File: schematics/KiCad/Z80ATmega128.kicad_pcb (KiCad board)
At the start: 2 copper layers, 139.7 x 100.3 mm, 90 parts, among them J1 AVR-ISP-6, J2 Serial I/O, J3 DC 5V, J4 DC 5V, J5 Z80[1..20], J6 Micro_SD_Card_Det_Hirose_DM3AT, J7 Z80[21..40], SW1 RESET, SW2 POWER, U1 74HC08, U10 74HC32, U11 74HC4050, U12 LP2950-3.3, U13 74HC74, U2 74HC04, U3 74HC125, U4 74AC573, U5 74HC574, U6 74HC125, U7 74HC244, U8 74HC245, U9 74HC32, Y1 16MHz, Y2 8MHz

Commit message: Update schematics for Z80 /HALT and /NMI.
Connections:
- CPU2 pad 16: unconnected-(CPU2-Pad16) -> /NMI
- CPU2 pad 17: unconnected-(CPU2-Pad17) -> /HALT

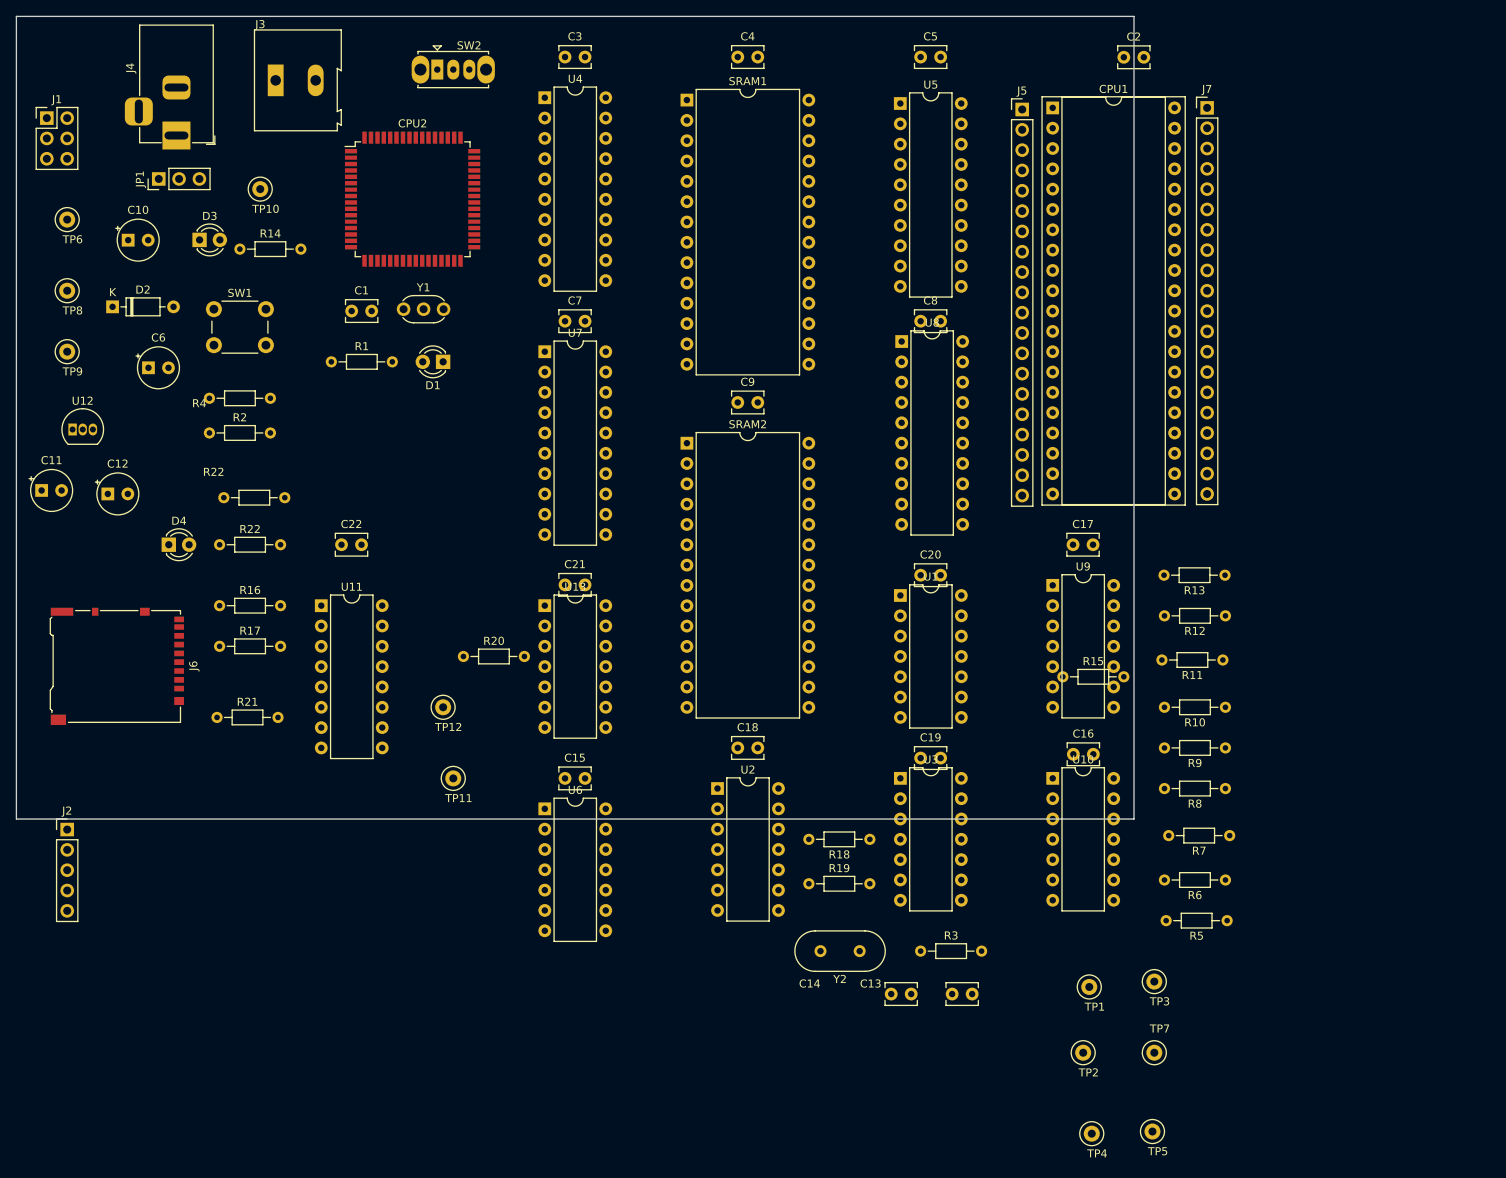
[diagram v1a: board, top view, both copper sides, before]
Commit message: Update schematics.
Separate reset and SD card interface as different layer.
Power on/manual reset are isolated from ISP /RST for stability.
XMEM /RD(PG1) and /WR(PG0) were swapped.
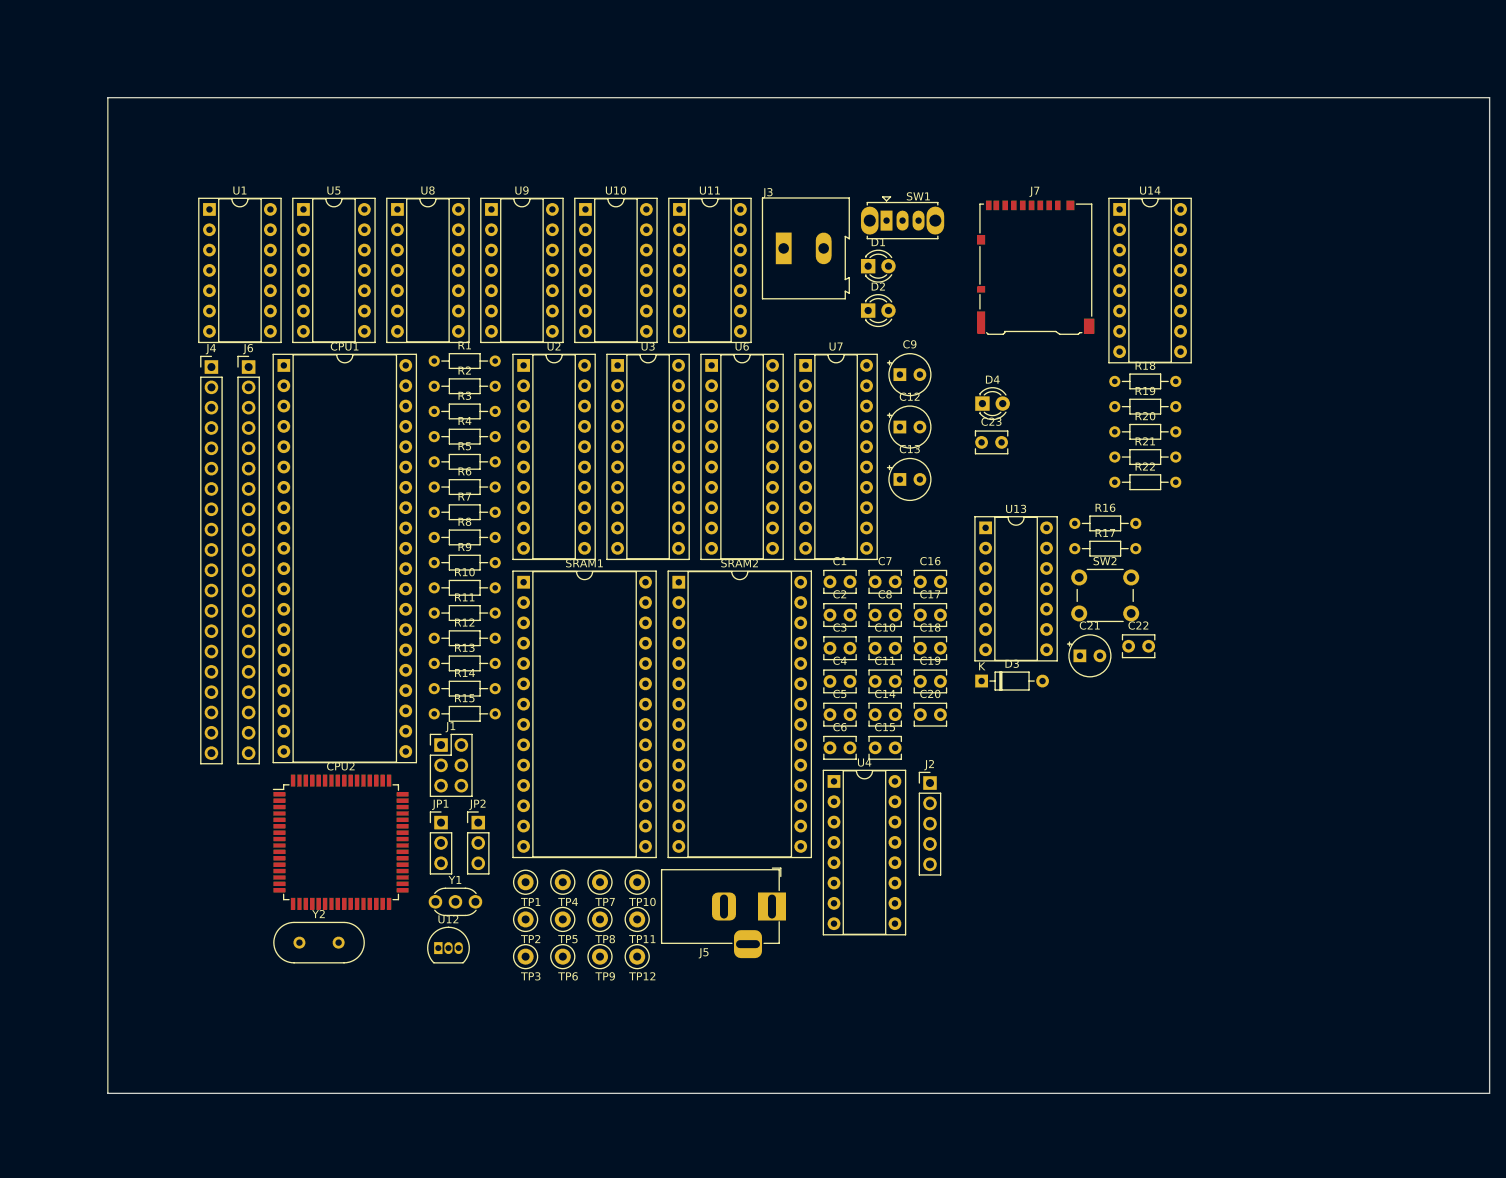
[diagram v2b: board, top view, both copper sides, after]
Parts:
- removed the R22 at (40.6, 81.3)
- removed the R22 at (41.2, 75.4)
- added C23: 0.1u, Capacitor_THT:C_Disc_D3.8mm_W2.6mm_P2.50mm, F.Cu at (135.9, 68.5)
- added JP2: DC-IN SEL, Connector_PinHeader_2.54mm:PinHeader_1x03_P2.54mm_Vertical, F.Cu at (73.0, 116.0)
- added R22: 1K, Resistor_THT:R_Axial_DIN0204_L3.6mm_D1.6mm_P7.62mm_Horizontal, F.Cu at (152.5, 73.5)
- added U14: 74HC4050, Package_DIP:DIP-16_W7.62mm_Socket, F.Cu at (153.1, 39.4)
- C10: value 100u -> 22p; footprint Capacitor_THT:CP_Radial_Tantal_D5.0mm_P2.50mm -> Capacitor_THT:C_Disc_D3.8mm_W2.6mm_P2.50mm
- C11: value 1u -> 22p; footprint Capacitor_THT:CP_Radial_Tantal_D5.0mm_P2.50mm -> Capacitor_THT:C_Disc_D3.8mm_W2.6mm_P2.50mm
- C13: value 22p -> 1u; footprint Capacitor_THT:C_Disc_D3.8mm_W2.6mm_P2.50mm -> Capacitor_THT:CP_Radial_Tantal_D5.0mm_P2.50mm
- C14: value 22p -> 0.1u
- C21: value 0.1u -> 47u; footprint Capacitor_THT:C_Disc_D3.8mm_W2.6mm_P2.50mm -> Capacitor_THT:CP_Radial_Tantal_D5.0mm_P2.50mm
- C6: value 1u -> 0.1u; footprint Capacitor_THT:CP_Radial_Tantal_D5.0mm_P2.50mm -> Capacitor_THT:C_Disc_D3.8mm_W2.6mm_P2.50mm
- C9: value 0.1u -> 100u; footprint Capacitor_THT:C_Disc_D3.8mm_W2.6mm_P2.50mm -> Capacitor_THT:CP_Radial_Tantal_D5.0mm_P2.50mm
- D1: value DMA -> POWER
- D2: value 1N4148 -> Z80 active; footprint Diode_THT:D_DO-35_SOD27_P7.62mm_Horizontal -> LED_THT:LED_D3.0mm
- D3: value POWER -> 1N4148; footprint LED_THT:LED_D3.0mm -> Diode_THT:D_DO-35_SOD27_P7.62mm_Horizontal
- J4: value DC 5V -> Z80[1..20]; footprint Connector_BarrelJack:BarrelJack_Horizontal -> Connector_PinHeader_2.54mm:PinHeader_1x20_P2.54mm_Vertical
- J5: value Z80[1..20] -> DC 5V; footprint Connector_PinHeader_2.54mm:PinHeader_1x20_P2.54mm_Vertical -> Connector_BarrelJack:BarrelJack_Horizontal
- J6: value Micro_SD_Card_Det_Hirose_DM3AT -> Z80[21..40]; footprint Connector_Card:microSD_HC_Hirose_DM3AT-SF-PEJM5 -> Connector_PinHeader_2.54mm:PinHeader_1x20_P2.54mm_Vertical
- J7: value Z80[21..40] -> Micro_SD_Card_Det_Hirose_DM3AT; footprint Connector_PinHeader_2.54mm:PinHeader_1x20_P2.54mm_Vertical -> Connector_Card:microSD_HC_Hirose_DM3AT-SF-PEJM5
- JP1: value DC-IN SEL -> Disable Z80
- R1: value 1K -> 10K
- R11, R15: value 10K -> 1K
- R13: value 10K -> 1M
- R14: value 1K -> 100
- R17: value 10K -> 100
- R18: value 1M -> 10K
- R19, R4: value 100 -> 10K
- SRAM1, SRAM2: footprint Package_DIP:DIP-28_W15.24mm -> Package_DIP:DIP-28_W15.24mm_Socket
- SW1: value RESET -> POWER; footprint Button_Switch_THT:SW_PUSH_6mm_H7.3mm -> Button_Switch_THT:SW_Slide_1P2T_CK_OS102011MS2Q
- SW2: value POWER -> RESET; footprint Button_Switch_THT:SW_Slide_1P2T_CK_OS102011MS2Q -> Button_Switch_THT:SW_PUSH_6mm_H7.3mm
- TP10: value /INTRQ -> /CLRWAIT
- TP12: value /CLRWAIT -> 3.3V
- TP6: value 5V -> /IORD
- TP7: value /IORD -> 5V
- TP8: value GND -> /INTRQ
- TP9: value 3.3V -> GND
- U1: value 74HC08 -> 74HC125; footprint Package_DIP:DIP-14_W7.62mm -> Package_DIP:DIP-14_W7.62mm_Socket
- U10: footprint Package_DIP:DIP-14_W7.62mm -> Package_DIP:DIP-14_W7.62mm_Socket
- U11: value 74HC4050 -> 74HC74; footprint Package_DIP:DIP-16_W7.62mm -> Package_DIP:DIP-14_W7.62mm_Socket
- U13: value 74HC74 -> 74HC132; footprint Package_DIP:DIP-14_W7.62mm -> Package_DIP:DIP-14_W7.62mm_Socket
- U2: value 74HC04 -> 74AC573; footprint Package_DIP:DIP-14_W7.62mm -> Package_DIP:DIP-20_W7.62mm_Socket
- U3: value 74HC125 -> 74HC574; footprint Package_DIP:DIP-14_W7.62mm -> Package_DIP:DIP-20_W7.62mm_Socket
- U4: value 74AC573 -> 74HC04; footprint Package_DIP:DIP-20_W7.62mm -> Package_DIP:DIP-16_W7.62mm_Socket
- U5: value 74HC574 -> 74HC125; footprint Package_DIP:DIP-20_W7.62mm -> Package_DIP:DIP-14_W7.62mm_Socket
- U6: value 74HC125 -> 74HC244; footprint Package_DIP:DIP-14_W7.62mm -> Package_DIP:DIP-20_W7.62mm_Socket
- U7: value 74HC244 -> 74HC245; footprint Package_DIP:DIP-20_W7.62mm -> Package_DIP:DIP-20_W7.62mm_Socket
- U8: value 74HC245 -> 74HC32; footprint Package_DIP:DIP-20_W7.62mm -> Package_DIP:DIP-14_W7.62mm_Socket
- U9: value 74HC32 -> 74HC08; footprint Package_DIP:DIP-14_W7.62mm -> Package_DIP:DIP-14_W7.62mm_Socket
- moved R21 116.8 mm to (152.5, 70.3)
- moved R5 114.5 mm to (67.5, 70.9), turned to 0 degrees
- moved D3 112.2 mm to (135.9, 98.3)
- moved TP6 111.0 mm to (83.5, 132.8)
- moved R6 110.4 mm to (67.5, 74.1), turned to 0 degrees
- moved J2 108.0 mm to (129.4, 111.1)
- moved R17 107.6 mm to (147.5, 81.8)
- moved R16 107.4 mm to (147.5, 78.6)
- moved R7 107.3 mm to (67.5, 77.2), turned to 0 degrees
- moved C11 106.9 mm to (122.6, 98.4)
- moved C10 106.4 mm to (122.6, 94.2)
- moved J5 104.4 mm to (109.7, 126.5)
- moved R8 103.8 mm to (67.5, 80.4), turned to 0 degrees
- moved D4 103.2 mm to (136.0, 63.6)
- moved TP8 103.0 mm to (88.2, 128.1)
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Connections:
- C10 pad 1: VCC -> Net-(C10-Pad1)
- C11 pad 1: VCC -> Net-(C11-Pad1)
- C12 pad 1: +3.3V -> VCC
- C13 pad 1: Net-(C13-Pad1) -> +3.3V
- C14 pad 1: Net-(C14-Pad1) -> VCC
- C21 pad 1: VCC -> Net-(D3-A)
- C22 pad 1: +3.3V -> VCC
- C6 pad 1: Net-(C6-Pad1) -> GND
- C6 pad 2: GND -> VCC
- C9 pad 1: GND -> VCC
- C9 pad 2: VCC -> GND
- CPU1 pad 23: Net-(CPU1-Pad23) -> Net-(CPU1-~{BUSACK})
- CPU1 pad 25: /BUSRQ -> Net-(CPU1-~{BUSRQ})
- CPU1 pad 26: /RESET -> /Z80_RESET
- CPU2 pad 15: /XRESET -> /Reset//Z80_SWRST
- CPU2 pad 2: Net-(CPU2-Pad2) -> Net-(CPU2-PE0)
- CPU2 pad 20: Net-(C6-Pad1) -> /Reset//AVR_RST
- CPU2 pad 3: Net-(CPU2-Pad3) -> Net-(CPU2-PE1)
- CPU2 pad 35: Net-(CPU2-Pad35) -> Net-(CPU2-PC0)
- CPU2 pad 36: Net-(CPU2-Pad36) -> Net-(CPU2-PC1)
- CPU2 pad 37: Net-(CPU2-Pad37) -> Net-(CPU2-PC2)
- CPU2 pad 38: Net-(CPU2-Pad38) -> Net-(CPU2-PC3)
- CPU2 pad 39: Net-(CPU2-Pad39) -> Net-(CPU2-PC4)
- CPU2 pad 40: Net-(CPU2-Pad40) -> Net-(CPU2-PC5)
- CPU2 pad 41: Net-(CPU2-Pad41) -> Net-(CPU2-PC6)
- CPU2 pad 42: Net-(CPU2-Pad42) -> Net-(CPU2-PC7)
- D1 pad 1: Net-(D1-Pad1) -> GND
- D1 pad 2: Net-(D1-Pad2) -> Net-(D1-A)
- D2 pad 1: VCC -> Net-(D2-K)
- D2 pad 2: Net-(C6-Pad1) -> Net-(D2-A)
- D3 pad 1: GND -> VCC
- D3 pad 2: Net-(D3-Pad2) -> Net-(D3-A)
- D4 pad 1: Net-(D4-Pad1) -> Net-(D4-K)
- J1 pad 1: Net-(CPU2-Pad3) -> Net-(CPU2-PE1)
- J1 pad 3: Net-(J1-Pad3) -> Net-(J1-SCK)
- J1 pad 4: Net-(CPU2-Pad2) -> Net-(CPU2-PE0)
- J1 pad 5: Net-(C6-Pad1) -> /Reset//ISP_RST
- J2 pad 1: Net-(J2-Pad1) -> Net-(J2-Pin_1)
- J2 pad 2: Net-(J2-Pad2) -> Net-(J2-Pin_2)
- J3 pad 2: Net-(J3-Pad2) -> Net-(J3-Pin_2)
- J4 pad 1: Net-(J4-Pad1) -> A11
- J4 pad 2: GND -> A12
- J4 pad 3: (no net) -> A13
- J5 pad 1: A11 -> Net-(J5-In)
- J5 pad 2: A12 -> GND
- J5 pad 3: A13 -> (no net)
- J6 pad 1: unconnected-(J6-Pad1) -> A10
- J6 pad 10: GND -> A1
- J6 pad 11: unconnected-(J6-Pad11) -> A0
- J6 pad 2: Net-(D4-Pad1) -> A9
- J6 pad 3: Net-(J6-Pad3) -> A8
- J6 pad 4: +3.3V -> A7
- J6 pad 5: Net-(J6-Pad5) -> A6
- J6 pad 6: GND -> A5
- J6 pad 7: MISO -> A4
- J6 pad 8: unconnected-(J6-Pad8) -> A3
- J6 pad 9: SW -> A2
- J7 pad 1: A10 -> unconnected-(J7-DAT2-Pad1)
- J7 pad 10: A1 -> GND
- J7 pad 11: A0 -> unconnected-(J7-SHIELD-Pad11)
- J7 pad 2: A9 -> Net-(D4-K)
- J7 pad 3: A8 -> Net-(J7-CMD)
- J7 pad 4: A7 -> +3.3V
- J7 pad 5: A6 -> Net-(J7-CLK)
- J7 pad 6: A5 -> GND
- J7 pad 7: A4 -> MISO
- J7 pad 8: A3 -> unconnected-(J7-DAT1-Pad8)
- J7 pad 9: A2 -> SW
- JP1 pad 1: Net-(J4-Pad1) -> GND
- JP1 pad 2: Net-(JP1-Pad2) -> Net-(CPU1-~{BUSRQ})
- JP1 pad 3: Net-(J3-Pad2) -> /BUSRQ
- R1 pad 2: Net-(D1-Pad2) -> /Reset//ISP_RST
- R10 pad 2: /RD -> Net-(CPU1-~{BUSACK})
- R11 pad 1: VCC -> Net-(D1-A)
- R11 pad 2: /WR -> VCC
- R12 pad 2: /BUSRQ -> /CLRWAIT
- R13 pad 1: VCC -> Net-(C11-Pad1)
- R13 pad 2: Net-(CPU1-Pad23) -> Net-(C10-Pad1)
- R14 pad 1: Net-(D3-Pad2) -> Net-(C11-Pad1)
- R14 pad 2: VCC -> Net-(R14-Pad2)
- R15 pad 2: SW -> Net-(D2-A)
- R16 pad 2: /SS -> Net-(D3-A)
- R17 pad 1: MOSI -> Net-(R17-Pad1)
- R17 pad 2: GND -> Net-(D3-A)
- R18 pad 1: Net-(C14-Pad1) -> VCC
- R18 pad 2: Net-(C13-Pad1) -> SW
- R19 pad 1: Net-(C14-Pad1) -> VCC
- R19 pad 2: Net-(R19-Pad2) -> /SS
- R2 pad 2: Net-(C6-Pad1) -> /NMI
- R20 pad 1: VCC -> MOSI
- R20 pad 2: /CLRWAIT -> GND
- R3 pad 2: /XRESET -> /XINT
- R4 pad 1: Net-(R4-Pad1) -> VCC
- R4 pad 2: Net-(C6-Pad1) -> /MREQ
- R5 pad 2: /NMI -> /IORQ
- R6 pad 2: /XINT -> /M1
- R7 pad 2: /MREQ -> /RD
- R8 pad 2: /IORQ -> /WR
- R9 pad 2: /M1 -> Net-(CPU1-~{BUSRQ})
- SRAM1 pad 22: Net-(SRAM1-Pad22) -> Net-(SRAM1-~{OE})
- SRAM1 pad 27: Net-(SRAM1-Pad27) -> Net-(SRAM1-~{WE})
- SRAM2 pad 20: Net-(SRAM2-Pad20) -> Net-(SRAM2-~{CS})
- SRAM2 pad 22: Net-(SRAM1-Pad22) -> Net-(SRAM1-~{OE})
- SRAM2 pad 27: Net-(SRAM1-Pad27) -> Net-(SRAM1-~{WE})
- SW1 pad 1: GND -> unconnected-(SW1-A-Pad1)
- SW1 pad 2: Net-(R4-Pad1) -> Net-(JP2-C)
- SW2 pad 1: unconnected-(SW2-Pad1) -> GND
- SW2 pad 2: Net-(JP1-Pad2) -> Net-(R17-Pad1)
- TP1 pad 1: Net-(TP1-Pad1) -> Net-(U3-OE)
- TP10 pad 1: /INTRQ -> /CLRWAIT
- TP12 pad 1: /CLRWAIT -> +3.3V
- TP3 pad 1: Net-(TP3-Pad1) -> Net-(U7-CE)
- TP4 pad 1: Net-(SRAM1-Pad27) -> Net-(SRAM1-~{WE})
- TP5 pad 1: Net-(SRAM1-Pad22) -> Net-(SRAM1-~{OE})
- TP6 pad 1: VCC -> /IORD
- TP7 pad 1: /IORD -> VCC
- TP8 pad 1: GND -> /INTRQ
- TP9 pad 1: +3.3V -> GND
- U1 pad 1: /WAIT -> Net-(U1-Pad1)
- U1 pad 10: /INTRQ -> GND
- U1 pad 11: /RESET -> SCK
- U1 pad 12: Net-(C6-Pad1) -> Net-(J1-SCK)
- U1 pad 13: /XRESET -> /Reset//ISP_RST
- U1 pad 2: 4MHz -> Net-(U1-Pad2)
- U1 pad 3: Net-(U1-Pad3) -> Net-(SRAM1-~{WE})
- U1 pad 4: /IOWR -> Net-(U1-Pad1)
- U1 pad 5: /MREQ -> Net-(U1-Pad5)
- U1 pad 6: Net-(TP3-Pad1) -> Net-(SRAM1-~{OE})
- U1 pad 8: Net-(TP1-Pad1) -> /BUSACK
- U1 pad 9: /IORD -> Net-(CPU1-~{BUSACK})
- U10 pad 3: Net-(U10-Pad3) -> Net-(U1-Pad2)
- U10 pad 6: Net-(U10-Pad6) -> Net-(U1-Pad5)
- U11 pad 1: +3.3V -> VCC
- U11 pad 10: Net-(R22-Pad1) -> /CLRWAIT
- U11 pad 11: GND -> Net-(U11B-C)
- U11 pad 12: unconnected-(U11-Pad12) -> Net-(U11B-D)
- U11 pad 13: (no net) -> VCC
- U11 pad 14: GND -> VCC
- U11 pad 2: Net-(D4-Pad1) -> Net-(U11A-D)
- U11 pad 3: /SS -> Net-(U11A-C)
- U11 pad 4: Net-(J6-Pad3) -> VCC
- U11 pad 5: MOSI -> 4MHz
- U11 pad 6: Net-(J6-Pad5) -> Net-(U11A-D)
- U11 pad 7: SCK -> GND
- U11 pad 8: GND -> Net-(U11B-~{Q})
- U11 pad 9: SCK -> /WAIT
- U13 pad 1: VCC -> Net-(D3-A)
- U13 pad 10: /CLRWAIT -> Net-(U13-Pad10)
- U13 pad 11: Net-(U1-Pad3) -> /Reset//AVR_RST
- U13 pad 13: VCC -> Net-(U13-Pad12)
- U13 pad 2: Net-(U13-Pad2) -> Net-(D3-A)
- U13 pad 4: VCC -> Net-(U13-Pad3)
- U13 pad 5: 4MHz -> Net-(U13-Pad3)
- U13 pad 6: Net-(U13-Pad2) -> Net-(U13-Pad10)
- U13 pad 8: Net-(U13-Pad8) -> Net-(U13-Pad12)
- U13 pad 9: /WAIT -> /Reset//ISP_RST
- U2 pad 10: Net-(U13-Pad3) -> GND
- U2 pad 11: Net-(R19-Pad2) -> /ALE
- U2 pad 12: Net-(D1-Pad1) -> A7
- U2 pad 13: /BUSACK -> A6
- U2 pad 14: VCC -> A5
- U2 pad 2: Net-(U2-Pad2) -> D0
- U2 pad 3: A15 -> D1
- U2 pad 4: Net-(SRAM2-Pad20) -> D2
- U2 pad 5: Net-(C6-Pad1) -> D3
- U2 pad 6: Net-(U2-Pad6) -> D4
- U2 pad 7: GND -> D5
- U2 pad 8: Net-(C14-Pad1) -> D6
- U2 pad 9: Net-(C13-Pad1) -> D7
- U3 pad 1: Net-(U2-Pad2) -> Net-(U3-OE)
- U3 pad 11: SCK -> /WAIT
- U3 pad 12: Net-(J1-Pad3) -> DB7
- U3 pad 13: Net-(C6-Pad1) -> DB6
- U3 pad 14: VCC -> DB5
- U3 pad 2: Net-(U10-Pad3) -> D0
- U3 pad 3: Net-(SRAM1-Pad27) -> D1
- U3 pad 4: Net-(U2-Pad2) -> D2
- U3 pad 5: Net-(U10-Pad6) -> D3
- U3 pad 6: Net-(SRAM1-Pad22) -> D4
- U3 pad 7: GND -> D5
- U3 pad 8: /BUSACK -> D6
- U3 pad 9: Net-(CPU1-Pad23) -> D7
- U4 pad 10: GND -> Net-(U11A-C)
- U4 pad 11: /ALE -> Net-(R14-Pad2)
- U4 pad 12: A7 -> Net-(D2-K)
- U4 pad 13: A6 -> /BUSACK
- U4 pad 14: A5 -> VCC
- U4 pad 15: A4 -> (no net)
- U4 pad 16: A3 -> (no net)
- U4 pad 2: D0 -> Net-(U1-Pad1)
- U4 pad 3: D1 -> A15
- U4 pad 4: D2 -> Net-(SRAM2-~{CS})
- U4 pad 5: D3 -> /Reset//ISP_RST
- U4 pad 6: D4 -> Net-(U4-Pad6)
- U4 pad 7: D5 -> GND
- U4 pad 8: D6 -> Net-(C11-Pad1)
- U4 pad 9: D7 -> Net-(C10-Pad1)
- U5 pad 1: Net-(TP1-Pad1) -> Net-(U4-Pad6)
- U5 pad 10: GND -> /BUSACK
- U5 pad 11: /WAIT -> Net-(SRAM1-~{OE})
- U5 pad 12: DB7 -> /RD
- U5 pad 13: DB6 -> /BUSACK
- U5 pad 14: DB5 -> VCC
- U5 pad 2: D0 -> Net-(J2-Pin_1)
- U5 pad 3: D1 -> Net-(CPU2-PE0)
- U5 pad 4: D2 -> Net-(U4-Pad6)
- U5 pad 5: D3 -> Net-(CPU2-PE1)
- U5 pad 6: D4 -> Net-(J2-Pin_2)
- U5 pad 7: D5 -> GND
- U5 pad 8: D6 -> Net-(SRAM1-~{WE})
- U5 pad 9: D7 -> /WR
- U6 pad 1: Net-(U2-Pad6) -> /BUSACK
- U6 pad 10: /BUSACK -> GND
- U6 pad 11: Net-(SRAM1-Pad27) -> Net-(CPU2-PC7)
- U6 pad 12: /WR -> A11
- U6 pad 13: /BUSACK -> Net-(CPU2-PC6)
- U6 pad 14: VCC -> A10
- U6 pad 2: Net-(J2-Pad1) -> Net-(CPU2-PC0)
- U6 pad 3: Net-(CPU2-Pad2) -> A12
- U6 pad 4: Net-(U2-Pad6) -> Net-(CPU2-PC1)
- U6 pad 5: Net-(CPU2-Pad3) -> A13
- U6 pad 6: Net-(J2-Pad2) -> Net-(CPU2-PC2)
- U6 pad 7: GND -> A14
- U6 pad 8: Net-(SRAM1-Pad22) -> Net-(CPU2-PC3)
- U6 pad 9: /RD -> A15
- U7 pad 1: /BUSACK -> /WR
- U7 pad 11: Net-(CPU2-Pad42) -> DB7
- U7 pad 12: A11 -> DB6
- U7 pad 13: Net-(CPU2-Pad41) -> DB5
- U7 pad 14: A10 -> DB4
- U7 pad 15: Net-(CPU2-Pad40) -> DB3
- U7 pad 16: A9 -> DB2
- U7 pad 17: Net-(CPU2-Pad39) -> DB1
- U7 pad 18: A8 -> DB0
- U7 pad 19: /BUSACK -> Net-(U7-CE)
- U7 pad 2: Net-(CPU2-Pad35) -> D0
- U7 pad 3: A12 -> D1
- U7 pad 4: Net-(CPU2-Pad36) -> D2
- U7 pad 5: A13 -> D3
- U7 pad 6: Net-(CPU2-Pad37) -> D4
- U7 pad 7: A14 -> D5
- U7 pad 8: Net-(CPU2-Pad38) -> D6
- U7 pad 9: A15 -> D7
- U8 pad 1: /WR -> A7
- U8 pad 10: GND -> Net-(U11B-~{Q})
- U8 pad 11: DB7 -> unconnected-(U8-Pad11)
- U8 pad 12: DB6 -> GND
- U8 pad 13: DB5 -> GND
- U8 pad 14: DB4 -> VCC
- U8 pad 2: D0 -> /IORQ
- U8 pad 3: D1 -> Net-(U10-Pad10)
- U8 pad 4: D2 -> /M1
- U8 pad 5: D3 -> /IORQ
- U8 pad 6: D4 -> /INTRQ
- U8 pad 7: D5 -> GND
- U8 pad 8: D6 -> Net-(U11B-D)
- U8 pad 9: D7 -> /IORQ
- U9 pad 1: A7 -> /WAIT
- U9 pad 10: Net-(U13-Pad8) -> /INTRQ
- U9 pad 11: unconnected-(U9-Pad11) -> /Z80_RESET
- U9 pad 12: GND -> Net-(U13-Pad10)
- U9 pad 13: GND -> /Reset//Z80_SWRST
- U9 pad 2: /IORQ -> 4MHz
- U9 pad 3: Net-(U10-Pad10) -> Net-(U11B-C)
- U9 pad 4: /M1 -> /IOWR
- U9 pad 5: /IORQ -> /MREQ
- U9 pad 6: /INTRQ -> Net-(U7-CE)
- U9 pad 8: Net-(U13-Pad12) -> Net-(U3-OE)
- U9 pad 9: /IORQ -> /IORD
- Y2 pad 1: Net-(C13-Pad1) -> Net-(C10-Pad1)
- Y2 pad 2: Net-(C14-Pad1) -> Net-(C11-Pad1)
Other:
- board size 139.7 x 100.3 mm -> 172.7 x 124.5 mm

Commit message: 74HC574 and 245 are changed to 74HCT.
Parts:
- U3: value 74HC574 -> 74HCT574
- U7: value 74HC245 -> 74HCT245
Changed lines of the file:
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@@
         (effects (font (size 1 1) (thickness 0.15)))
     )
-    (fp_text value "74HC245" (at 3.81 25.19) (layer "F.Fab")
+    (fp_text value "74HCT245" (at 3.81 25.19) (layer "F.Fab")
         (effects (font (size 1 1) (thickness 0.15)))
     )
@@
         (effects (font (size 1 1) (thickness 0.15)))
     )
-    (fp_text value "74HC574" (at 3.81 25.19) (layer "F.Fab")
+    (fp_text value "74HCT574" (at 3.81 25.19) (layer "F.Fab")
         (effects (font (size 1 1) (thickness 0.15)))
     )

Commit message: Changed USB power line connection.
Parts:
- added J2: Serial0, Connector_PinHeader_2.54mm:PinHeader_1x06_P2.54mm_Vertical, F.Cu at (34.7, 118.1)
- added J3: Serial1, Connector_PinHeader_2.54mm:PinHeader_1x06_P2.54mm_Vertical, F.Cu at (39.4, 118.1)
- U4: footprint Package_DIP:DIP-16_W7.62mm_Socket -> Package_DIP:DIP-14_W7.62mm_Socket
- renumbered J3 to J4, J4 to J5, J5 to J6, J6 to J7, J7 to J8
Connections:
- net Net-(JP2-C) renamed VBUS
- U5 pad 2: Net-(J2-Pin_1) -> Net-(J2-Pin_2)
- U5 pad 6: Net-(J2-Pin_2) -> Net-(J2-Pin_3)
